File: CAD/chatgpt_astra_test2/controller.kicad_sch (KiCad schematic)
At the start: 22 parts, among them J4 USB-C, J5 UART / 3.3 V ONLY, SW1 RESET, SW2 BOOT, U4 ESP32-S3-WROOM-1-N8, U5 TPS3839G33DBZR, U6 USBLC6-2SC6

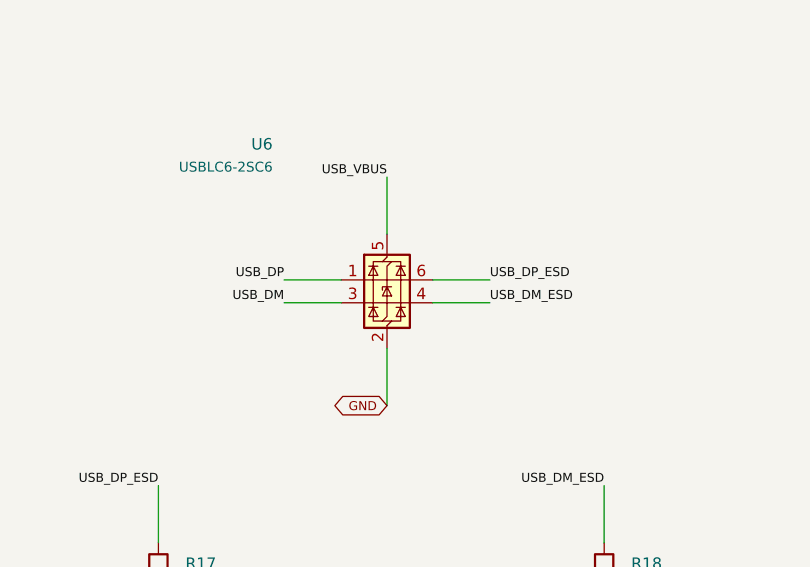
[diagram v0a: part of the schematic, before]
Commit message: Refine USB pair and add prototype thermal copper and stackup
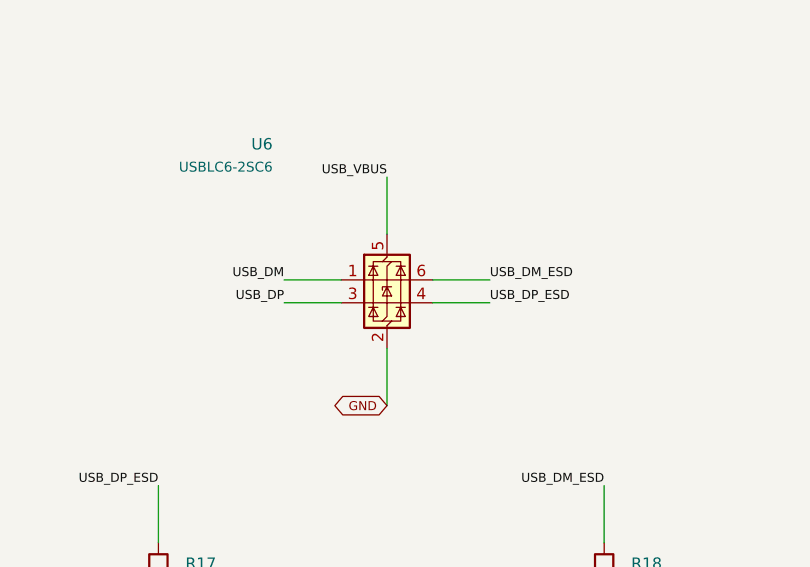
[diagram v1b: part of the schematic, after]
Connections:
- net USB_DM: now also U6.1 (I/O1); no longer U6.3 (I/O2)
- net USB_DM_ESD: now also U6.6 (I/O1); no longer U6.4 (I/O2)
- net USB_DP: now also U6.3 (I/O2); no longer U6.1 (I/O1)
- net USB_DP_ESD: now also U6.4 (I/O2); no longer U6.6 (I/O1)
